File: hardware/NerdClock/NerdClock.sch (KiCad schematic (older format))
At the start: 86 parts, among them J1 Conn_01x02, J10 Conn_01x04, J2 Jack-DC, J3 ICSP, J4 Conn_01x04, J5 Conn_01x03, J6 Conn_01x03, J7 USB_B_Micro, J8 Conn_01x02, J9 Conn_01x05, Q1 RTR025N03FRATL, Q2 RTR025N03FRATL, SW1 SW_MEC_5G, SW2 SW_MEC_5G, SW3 SW_MEC_5G, SW4 SW_MEC_5G, U1 IFX1117, U2 DRV8313, U3 ATmega168P-20AU, U4 DS1338Z-18+, U5 OPB706A, U6 CH340C, Y1 16MHz, Y2 32.768kHz/12.5pf

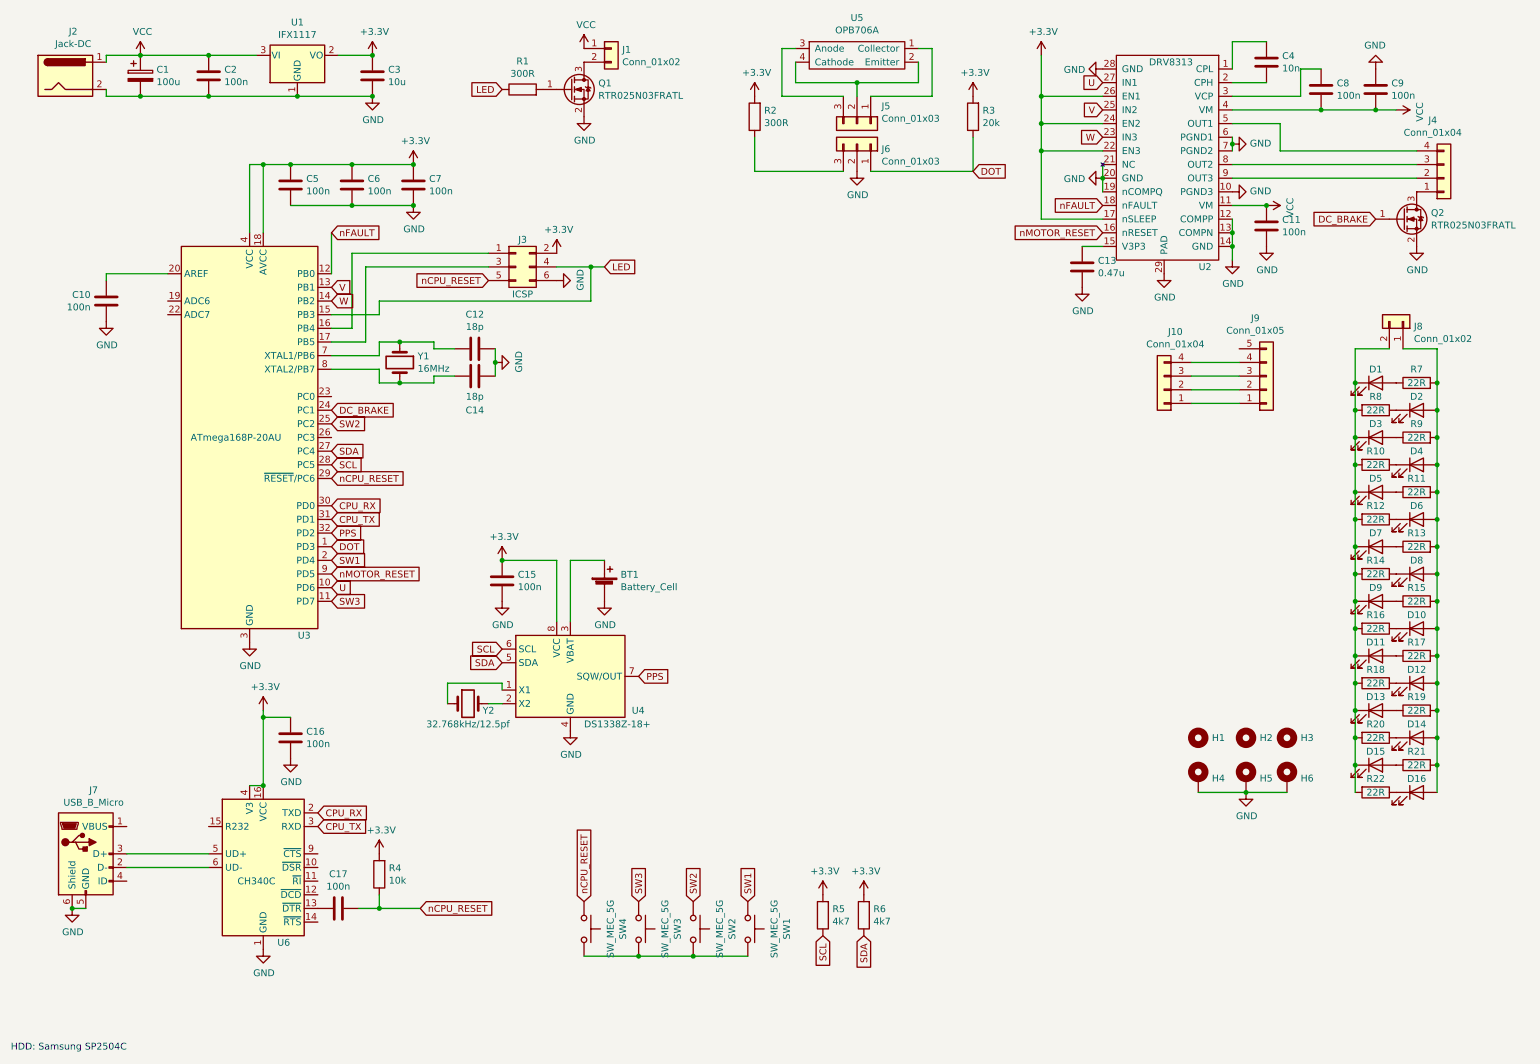
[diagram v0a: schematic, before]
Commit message: Put LEDs on the right side (wtffff)
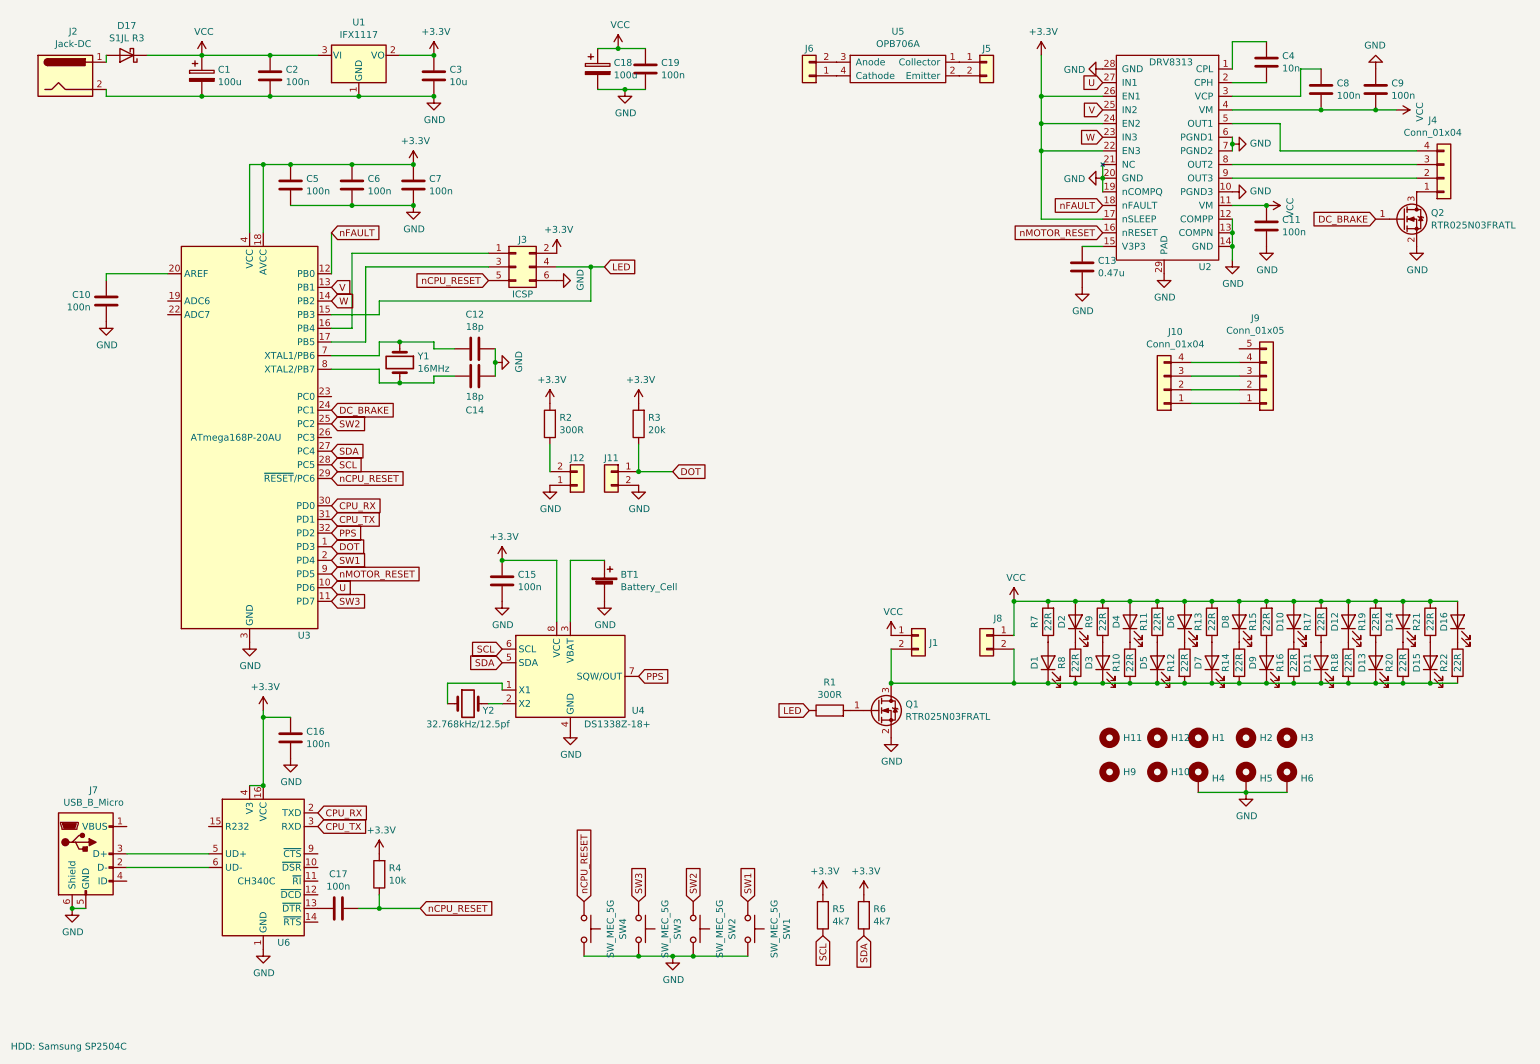
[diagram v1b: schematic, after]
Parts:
- removed J5, J6: Conn_01x03, Connector_PinHeader_2.54mm:PinHeader_1x03_P2.54mm_Vertical, symbol Connector_Generic:Conn_01x03
- added C18: 100u, Capacitor_SMD:CP_Elec_5x5.4, symbol Device:CP
- added C19: 100n, Capacitor_SMD:C_0603_1608Metric, symbol Device:C
- added D17: S1JL R3, Diode_SMD:D_SMA, symbol Diode:B120-E3
- added H10, H11, H12, H9: MountingHole, MountingHole:MountingHole_3.2mm_M3, symbol Mechanical:MountingHole
- added J11, J12, J5, J6: Conn_01x02, Connector_PinHeader_2.54mm:PinHeader_1x02_P2.54mm_Vertical, symbol Connector_Generic:Conn_01x02
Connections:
- net DOT: now also J11.1 (Pin_1)
- net GND: now also SW1.3 (B), SW1.4 (B), SW2.3 (B), SW2.4 (B), SW3.3 (B), SW3.4 (B), SW4.3 (B), SW4.4 (B), C18.2, C19.2, J11.2 (Pin_2), J12.1 (Pin_1)
- net VCC: now also D10.2 (A), D12.2 (A), D14.2 (A), D16.2 (A), D2.2 (A), D4.2 (A), D6.2 (A), D8.2 (A), J8.1 (Pin_1), R11.2, R13.2, R15.2, R17.2, R19.2, R21.2, R7.2, R9.2, C18.1, C19.1, D17.1 (K); no longer J2.1
- net at U5.1 (Collector): now also J5.1 (Pin_1)
- net at U5.2 (Emitter): now also J5.2 (Pin_2); no longer U5.4 (Cathode)
- net at U5.3 (Anode): now also J6.2 (Pin_2)
- net at R2.1: now also J12.2 (Pin_2)
- net at J1.2 (Pin_2), Q1.3 (D): now also D1.1 (K), D11.1 (K), D13.1 (K), D15.1 (K), D3.1 (K), D5.1 (K), D7.1 (K), D9.1 (K), J8.2 (Pin_2), R10.2, R12.2, R14.2, R16.2, R18.2, R20.2, R22.2, R8.2
- new net: D17.2 (A), J2.1
- new net: J6.1 (Pin_1), U5.4 (Cathode)
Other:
- moved on the sheet: C1, C2, C3, D1, D10, D11, D12, D13, D14, D15, D16, D2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

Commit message: Routing backup
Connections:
- net DC_BRAKE: now also U3.11 (PD7); no longer U3.24 (PC1)
- net SW3: now also U3.24 (PC1); no longer U3.11 (PD7)
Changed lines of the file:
@@
 Text GLabel 2750 3500 2    50   Input ~ 0
 SW2
-Text GLabel 2750 4800 2    50   Input ~ 0
+Text GLabel 2750 3400 2    50   Input ~ 0
 SW3
 $Comp
@@
 Text GLabel 10400 2000 0    50   Input ~ 0
 DC_BRAKE
-Text GLabel 2750 3400 2    50   Input ~ 0
+Text GLabel 2750 4800 2    50   Input ~ 0
 DC_BRAKE
 $Comp
@@
 	5250 7400 5000 7400
 $Comp
-L power:VCC #PWR?
+L power:VCC #PWR0105
 U 1 1 61EFF6FD
 P 7750 4800
-F 0 "#PWR?" H 7750 4650 50  0001 C CNN
+F 0 "#PWR0105" H 7750 4650 50  0001 C CNN
 F 1 "VCC" H 7765 4973 50  0000 C CNN
 F 2 "" H 7750 4800 50  0001 C CNN

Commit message: Routing probably done?
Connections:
- net SW3: now also U3.26 (PC3); no longer U3.24 (PC1)
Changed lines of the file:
@@
 Text GLabel 2750 3500 2    50   Input ~ 0
 SW2
-Text GLabel 2750 3400 2    50   Input ~ 0
+Text GLabel 2750 3600 2    50   Input ~ 0
 SW3
 $Comp

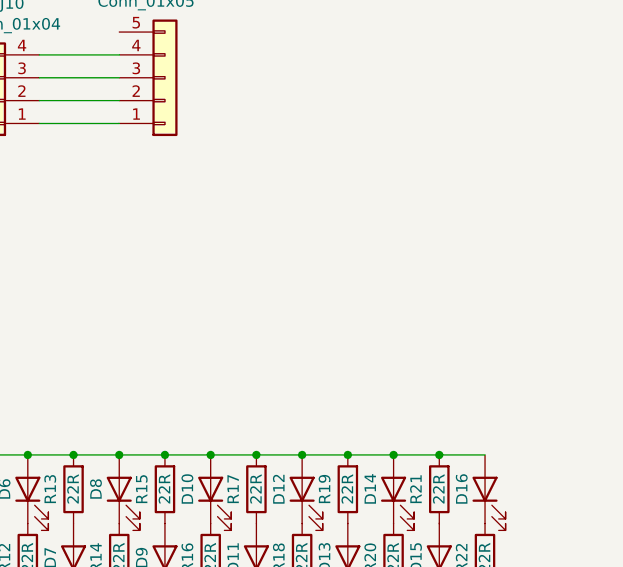
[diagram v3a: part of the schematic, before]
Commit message: Fix all DRC errors
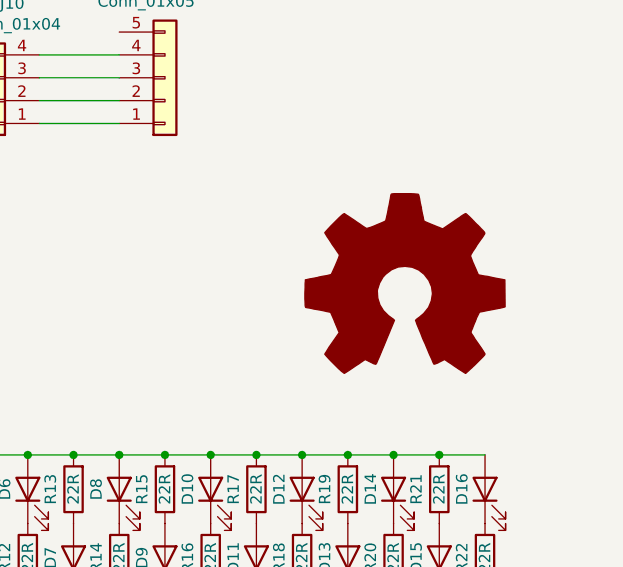
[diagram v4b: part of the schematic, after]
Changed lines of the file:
@@
 Connection ~ 7750 5400
 Connection ~ 6850 5400
+$Comp
+L Graphic:Logo_Open_Hardware_Large #LOGO?
+U 1 1 6210449D
+P 10650 4100
+F 0 "#LOGO?" H 10650 4600 50  0001 C CNN
+F 1 "Logo_Open_Hardware_Large" H 10650 3700 50  0001 C CNN
+F 2 "" H 10650 4100 50  0001 C CNN
+F 3 "~" H 10650 4100 50  0001 C CNN
+	1    10650 4100
+	1    0    0    -1
+$EndComp
 $EndSCHEMATC

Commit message: Off to JLCPCB!
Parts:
- added D18, D19: LED, WhiteLed1W:WhiteLed1W, symbol Device:LED
- added R23, R24: 22R, Resistor_SMD:R_0603_1608Metric, symbol Device:R
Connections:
- net +3V3: no longer U2.22 (EN3), U2.24 (EN2), U2.26 (EN1)
- net VCC: now also D18.2 (A), R23.2
- net EN_MOT: now reaches U3.23 (PC0)
- net EN_MOT: now also U2.22 (EN3), U2.24 (EN2), U2.26 (EN1)
- net at D1.1 (K), D11.1 (K), D13.1 (K)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: now also D19.1 (K), R24.2
- new net: D19.2 (A), R23.1
- new net: D18.1 (K), R24.1
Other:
- moved on the sheet: D1, D10, D11, D12, D13, D14, D15, D16, D2, D3, D4, D5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

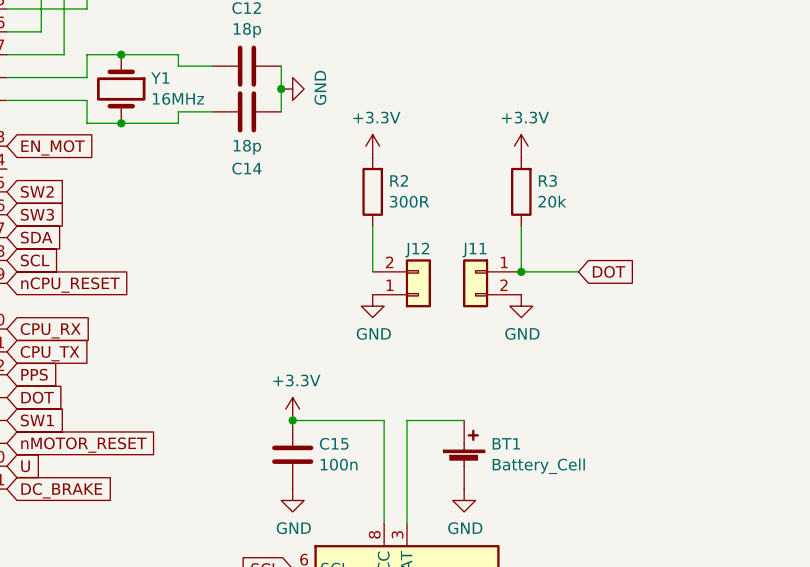
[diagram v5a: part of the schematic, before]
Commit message: Fixed hardware bug (polarity of IR led in relfection sensor
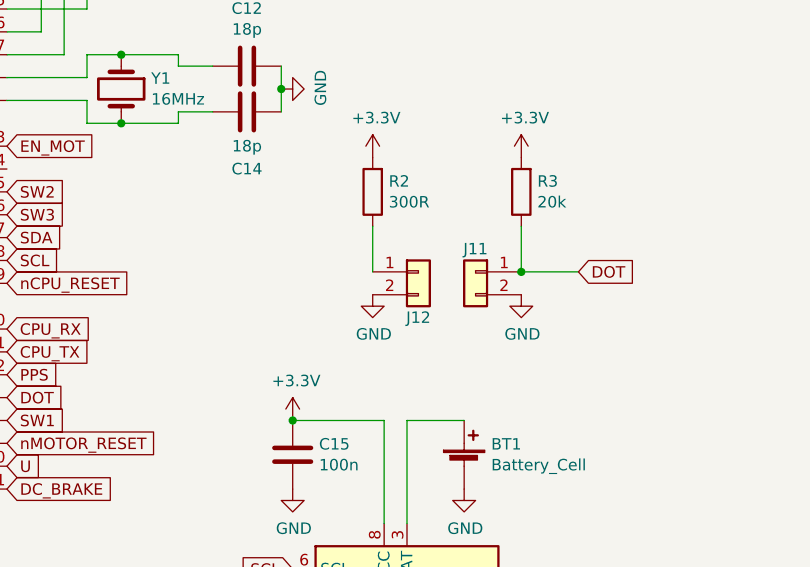
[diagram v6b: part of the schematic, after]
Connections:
- net GND: now also J12.2 (Pin_2); no longer J12.1 (Pin_1)
- net at R2.1: now also J12.1 (Pin_1); no longer J12.2 (Pin_2)
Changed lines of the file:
@@
 L Connector_Generic:Conn_01x02 J12
 U 1 1 619D28C8
-P 4550 3950
-F 0 "J12" H 4550 3750 50  0000 C CNN
-F 1 "Conn_01x02" H 4468 3716 50  0001 C CNN
-F 2 "Connector_PinHeader_2.54mm:PinHeader_1x02_P2.54mm_Vertical" H 4550 3950 50  0001 C CNN
-F 3 "~" H 4550 3950 50  0001 C CNN
-	1    4550 3950
-	1    0    0    1
+P 4550 3850
+F 0 "J12" H 4550 3650 50  0000 C CNN
+F 1 "Conn_01x02" H 4468 3616 50  0001 C CNN
+F 2 "Connector_PinHeader_2.54mm:PinHeader_1x02_P2.54mm_Vertical" H 4550 3850 50  0001 C CNN
+F 3 "~" H 4550 3850 50  0001 C CNN
+	1    4550 3850
+	1    0    0    -1
 $EndComp
 $Comp
